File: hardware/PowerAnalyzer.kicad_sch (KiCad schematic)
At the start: 59 parts, among them J1 EXPANSION, J10 TEST_IN, J11 PWR_IN, J12 PWR_OUT, J2 UDPI, J3 I2C, J4 FAN, J5 NTC, J6 UART, J7 USB_C_Receptacle_USB2.0_16P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

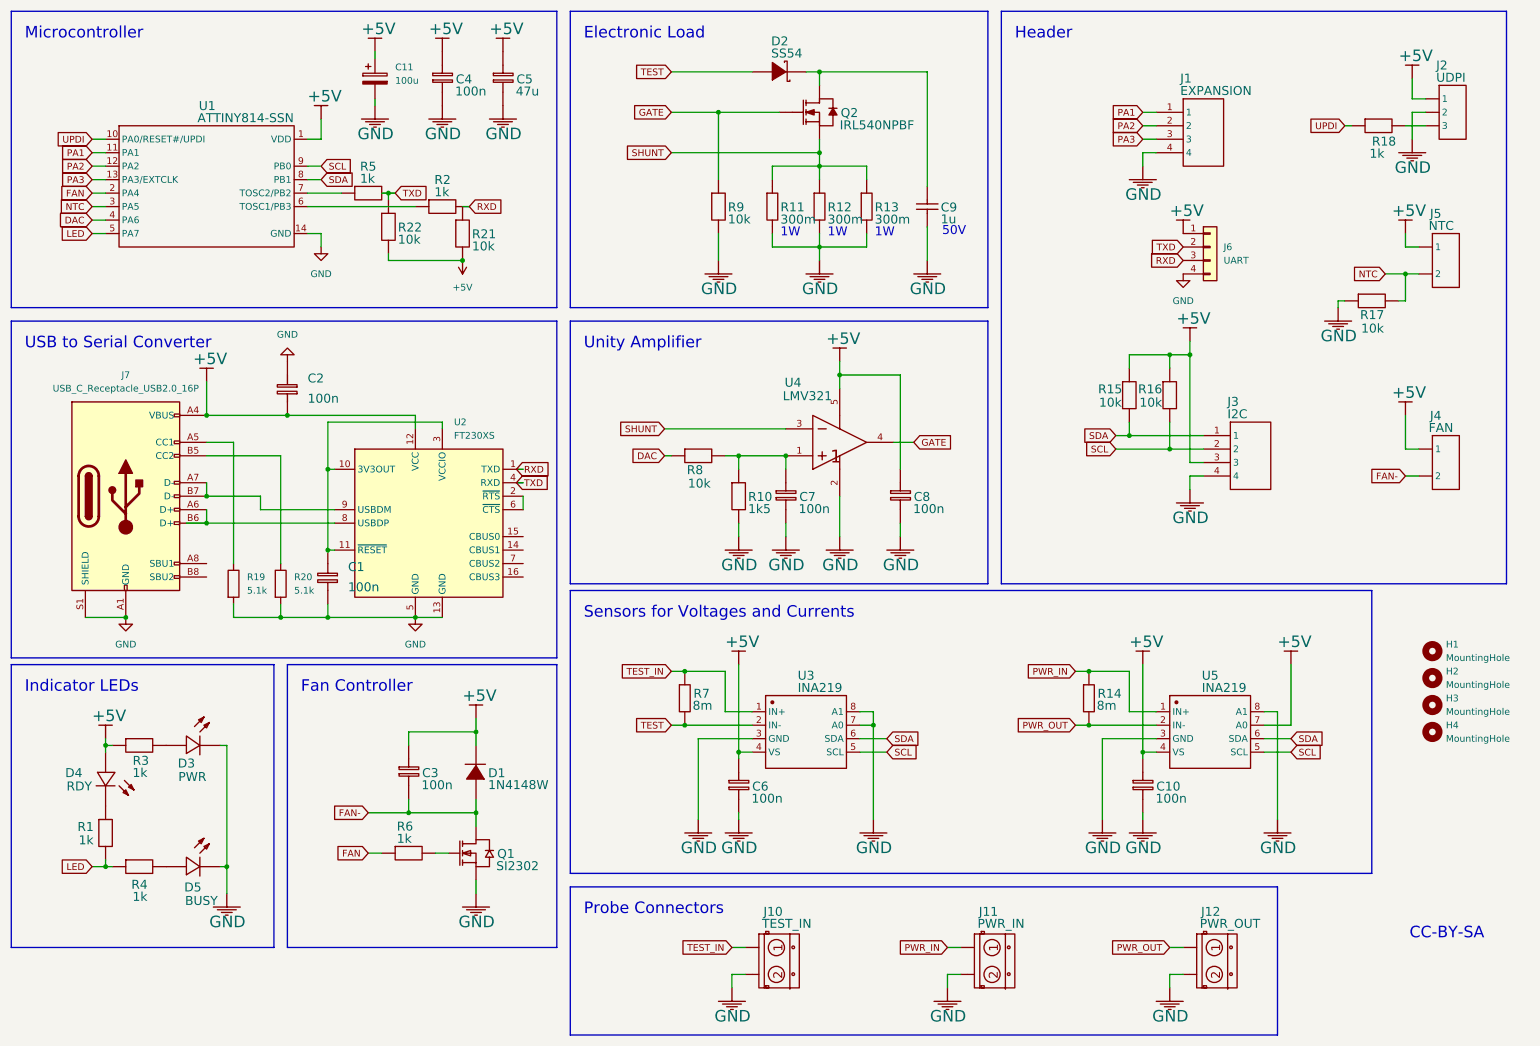
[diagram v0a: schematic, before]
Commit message: Fix diodes
Their pins are numbered differently on easyEDA.
Move some vias which may cause tombstoning.
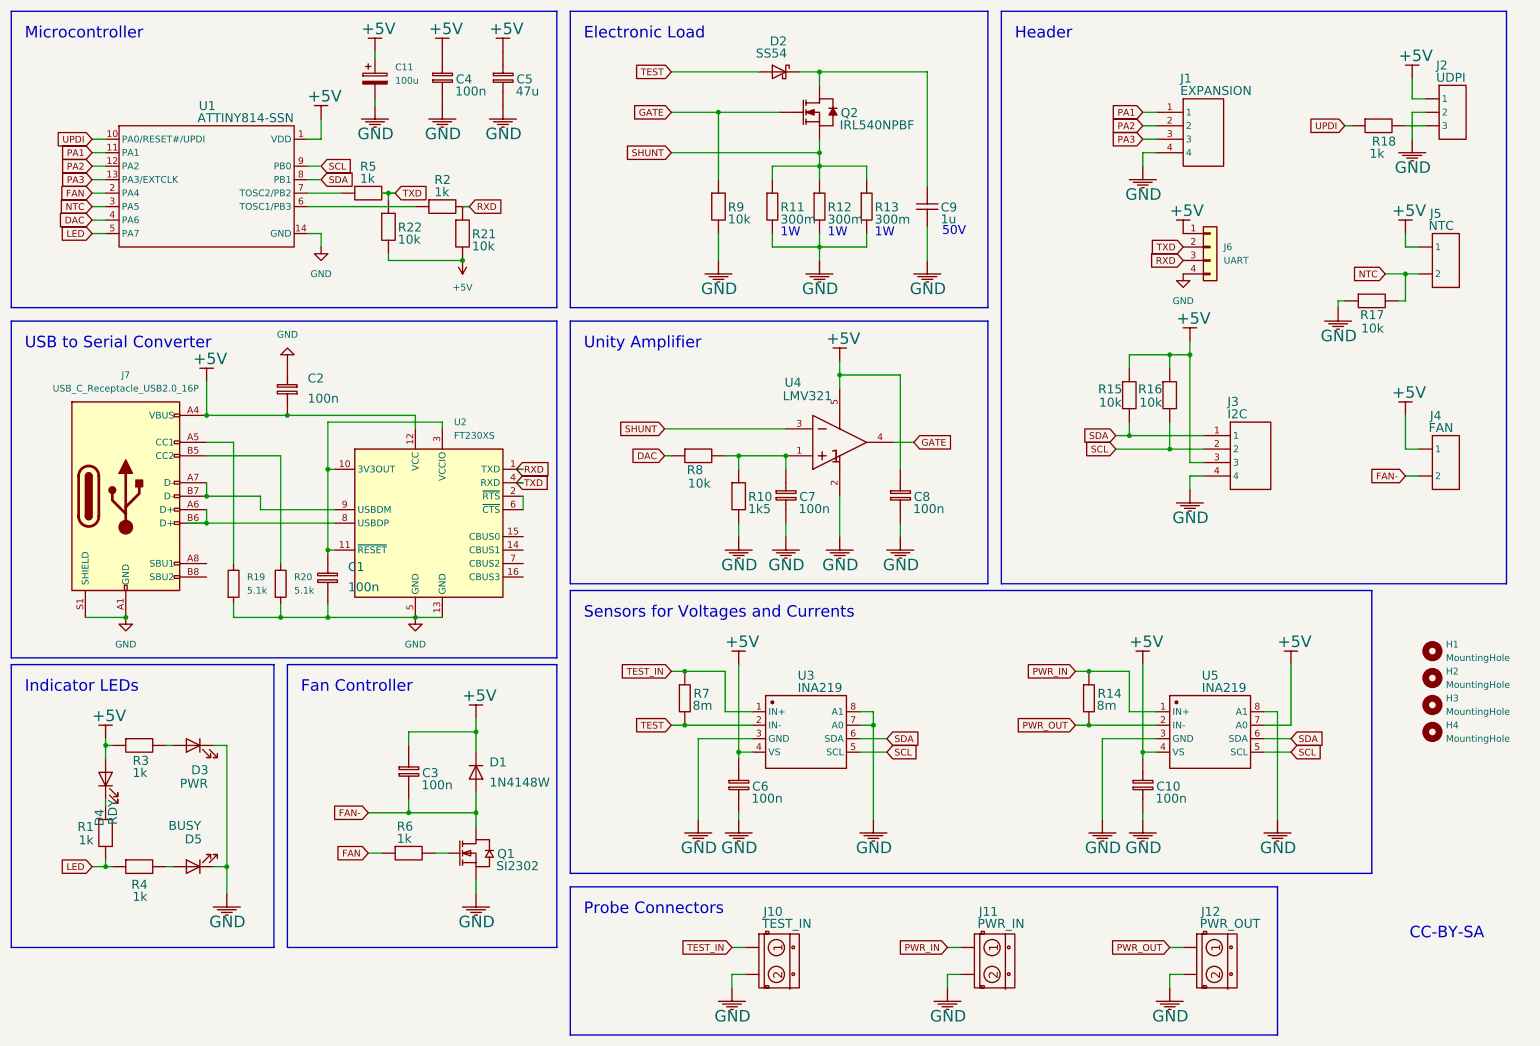
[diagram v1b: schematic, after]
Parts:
- D1: symbol Unknown_365_-270 -> Device:D
- D2: symbol SS54_C123946 -> Device:D_Schottky
- D3: symbol Unknown_155_-295 -> Device:LED
- D4: symbol Unknown_95_-265 -> Device:LED
- D5: symbol Unknown_155_-205 -> Device:LED
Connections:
- net +5V: now also D1.1 (K), D4.2 (A); no longer D1.2 (K), D4.1 (+)
- net FAN-: now also D1.2 (A); no longer D1.1 (A)
- net GND: now also D3.1 (K), D5.1 (K); no longer D3.2 (-), D5.2 (-)
- net TEST: now also D2.2 (A); no longer D2.1 (A)
- net at R3.2: now also D3.2 (A); no longer D3.1 (+)
- net at R1.2: now also D4.1 (K); no longer D4.2 (-)
- net at C9.2, Q2.2 (D): now also D2.1 (K); no longer D2.2 (K)
- net at R4.2: now also D5.2 (A); no longer D5.1 (+)

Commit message: Pocket Power Prowler v2
Migrate from semi-constant current control via shunt and operational
amplifier to direct DAC- and P[ID]-based control algorithm.
Bias the op amp just below the MOSFET threshold voltage to make use of
full DAC range.
Reduce DAC output capacitance from 100 n to 10 p (in order to filter out
high frequencies coming from DAC peripheral clock).

Shield the op amp and the fan controller.

Allow for powering the fan with external power.

Remove the series diode with the load, unsure for the reason of its
existance, but no literature seems to confirm the need for it.

Make the board a tad smaller.
Rebrand!
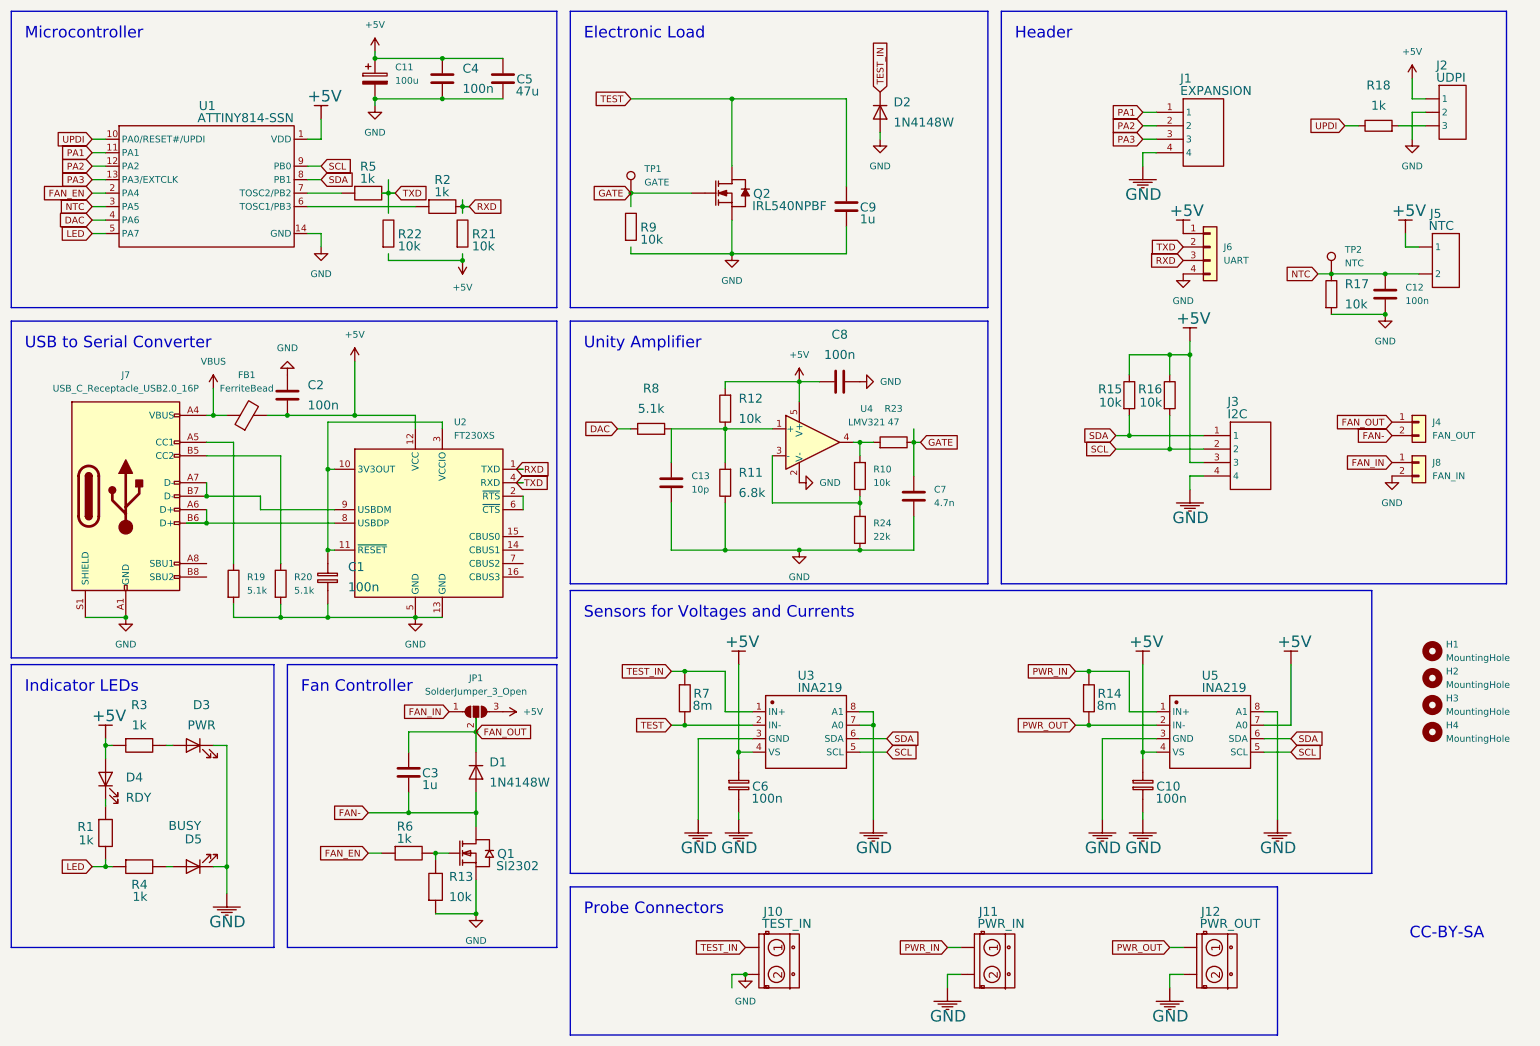
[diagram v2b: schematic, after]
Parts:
- removed C3: 100n, Capacitor_SMD:C_0603_1608Metric, symbol Cap_0603_EU_1
- removed C7: 100n, Capacitor_SMD:C_0603_1608Metric, symbol Cap_0603_EU_4
- removed D2: SS54, Diode_SMD:D_SMA, symbol Device:D_Schottky
- removed J4: FAN, Connector_PinHeader_2.54mm:PinHeader_1x02_P2.54mm_Vertical, symbol Header-Male-2.54_1x2_1
- removed R10: 1k5, Resistor_SMD:R_0603_1608Metric, symbol Res_0603(1/10W)_EU_12
- removed R11: 300m, Resistor_SMD:R_2512_6332Metric, symbol CR2512F0R3E04_2
- removed R12: 300m, Resistor_SMD:R_2512_6332Metric, symbol CR2512F0R3E04_1
- removed R13: 300m, Resistor_SMD:R_2512_6332Metric, symbol CR2512F0R3E04
- removed U4: LMV321, Package_TO_SOT_SMD:SOT-23-5, symbol LMV321B-TR
- added C12: 100n, Capacitor_SMD:C_0603_1608Metric, symbol Device:C
- added C13: 10p, Capacitor_SMD:C_0603_1608Metric, symbol Device:C
- added C3: 1u, Capacitor_SMD:C_0603_1608Metric, symbol Device:C
- added C7: 4.7n, Capacitor_SMD:C_0603_1608Metric, symbol Device:C
- added D2: 1N4148W, Diode_SMD:D_SOD-123, symbol Device:D
- added FB1: FerriteBead, Inductor_SMD:L_0603_1608Metric, symbol Device:FerriteBead
- added J4: FAN_OUT, Connector_PinHeader_2.54mm:PinHeader_1x02_P2.54mm_Vertical, symbol Connector_Generic:Conn_01x02
- added J8: FAN_IN, Connector_PinHeader_2.54mm:PinHeader_1x02_P2.54mm_Vertical, symbol Connector_Generic:Conn_01x02
- added JP1: SolderJumper_3_Open, Jumper:SolderJumper-3_P1.3mm_Open_RoundedPad1.0x1.5mm, symbol Jumper:SolderJumper_3_Open
- added R10, R12: 10k, Resistor_SMD:R_0603_1608Metric, symbol Device:R
- added R11: 6.8k, Resistor_SMD:R_0603_1608Metric, symbol Device:R
- added R13: 10k, Resistor_SMD:R_0603_1608Metric, symbol Res_0603(1/10W)_EU_5
- added R23: 47, Resistor_SMD:R_0603_1608Metric, symbol Device:R
- added R24: 22k, Resistor_SMD:R_0603_1608Metric, symbol Device:R
- added TP1: GATE, TestPoint:TestPoint_Pad_D1.0mm, symbol Connector:TestPoint
- added TP2: NTC, TestPoint:TestPoint_Pad_D1.0mm, symbol Connector:TestPoint
- added U4: LMV321, Package_TO_SOT_SMD:SOT-23-5, symbol Amplifier_Operational:LMV321
- C2: symbol Cap_0603_EU_2 -> Device:C
- C4: symbol Cap_0603_EU -> Device:C
- C5: symbol Cap_1206_EU -> Device:C
- C8: symbol Cap_0603_EU_7 -> Device:C
- C9: symbol UMK107AB7105KA-T -> Device:C; Voltage (none) -> 50V
- R15: symbol Res_0603(1/10W)_EU_6 -> Device:R
- R16: symbol Res_0603(1/10W)_EU_7 -> Device:R
- R17: symbol Res_0603(1/10W)_EU_10 -> Device:R
- R18: symbol Res_0603(1/10W)_EU_2 -> Device:R
- R21, R22, R9: symbol Res_0603(1/10W)_EU_3 -> Device:R
- R8: value 10k -> 5.1k; symbol Res_0603(1/10W)_EU_11 -> Device:R; Manufacturer UniOhm -> (none); Manufacturer Part 0603WAF1002T5E -> (none); Supplier LCSC -> (none); Supplier Part C25804 -> (none)
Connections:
- net SHUNT is gone; now on net GND: Q2.3 (S)
- net +5V: now also R15.1, R16.1, FB1.2, JP1.3 (B), R12.2, U4.5 (V+); no longer D1.1 (K), J7.A4 (VBUS), J7.A9 (VBUS), J7.B4 (VBUS), J7.B9 (VBUS), R15.2, R16.2, R21.1, R22.1
- net DAC: now also R8.1; no longer R8.2
- net FAN-: now also C3.2, J4.2 (Pin_2)
- net GATE: now also C7.1, R23.1, TP1.1; no longer R9.2
- net GND: now also C9.2, C12.1, C13.2, C7.2, D2.2 (A), J8.2 (Pin_2), R11.1, R13.1, R24.1, U4.2 (V-); no longer C9.1, R9.1
- net NTC: now also C12.2, TP2.1
- net RXD: no longer R21.2
- net SCL: now also R16.2; no longer R16.1
- net SDA: now also R15.2; no longer R15.1
- net TEST: now also C9.1, Q2.2 (D)
- net TEST_IN: now also D2.1 (K)
- net TXD: no longer R22.2
- net at Q1.1 (G), R6.2: now also R13.2
- net FAN renamed FAN_EN
- new net: C13.1, R11.2, R12.1, R8.2, U4.1 (+)
- new net: R10.1, R24.2, U4.3 (-)
- new net: R10.2, R23.2, U4.4
- new net FAN_IN: J8.1 (Pin_1), JP1.1 (A)
- new net FAN_OUT: C3.1, D1.1 (K), J4.1 (Pin_1), JP1.2 (C)
- new net VBUS: FB1.1, J7.A4 (VBUS), J7.A9 (VBUS), J7.B4 (VBUS), J7.B9 (VBUS)
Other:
- note removed: "1W"
- note removed: "50V"
- moved on the sheet: Q2

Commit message: Finish (?) KiCadifying
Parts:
- C1: symbol Cap_0603_EU_2 -> Device:C
- C10: symbol Cap_0603_EU_6 -> Device:C
- C6: symbol Cap_0603_EU_5 -> Device:C
- J1: symbol 220S-1*4P H=8.5MM Ytype Gold-plated_1 -> Connector_Generic:Conn_01x04
- J10: symbol Unknown_160_-100 -> Connector:Screw_Terminal_01x02
- J11: symbol Unknown_320_-100 -> Connector:Screw_Terminal_01x02
- J12: symbol Unknown_485_-100 -> Connector:Screw_Terminal_01x02
- J2: symbol Unknown_1085_-710 -> Connector_Generic:Conn_01x03
- J3: symbol 220S-1*4P H=8.5MM Ytype Gold-plated -> Connector_Generic:Conn_01x04
- J5: symbol Header-Male-2.54_1x2 -> Connector_Generic:Conn_01x02
- R1: symbol Res_0603(1/10W)_EU_4 -> Device:R
- R13, R6: symbol Res_0603(1/10W)_EU_5 -> Device:R
- R2: symbol Res_0603(1/10W)_EU_9 -> Device:R
- R3: symbol Res_0603(1/10W)_EU -> Device:R
- R4: symbol Res_0603(1/10W)_EU_1 -> Device:R
- R5: symbol Res_0603(1/10W)_EU_8 -> Device:R
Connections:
- net +5V: no longer C10.1, R3.1
- net GND: no longer C1.1, C10.2
- net LED: no longer R1.1, R4.1
- net at D3.2 (A): no longer R3.2
- net at D4.1 (K): no longer R1.2
- net at U2.10 (3V3OUT), U2.11 (~{RESET}), U2.3 (VCCIO): no longer C1.2
- net at D5.2 (A): no longer R4.2
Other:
- moved on the sheet: R18, R21, R22

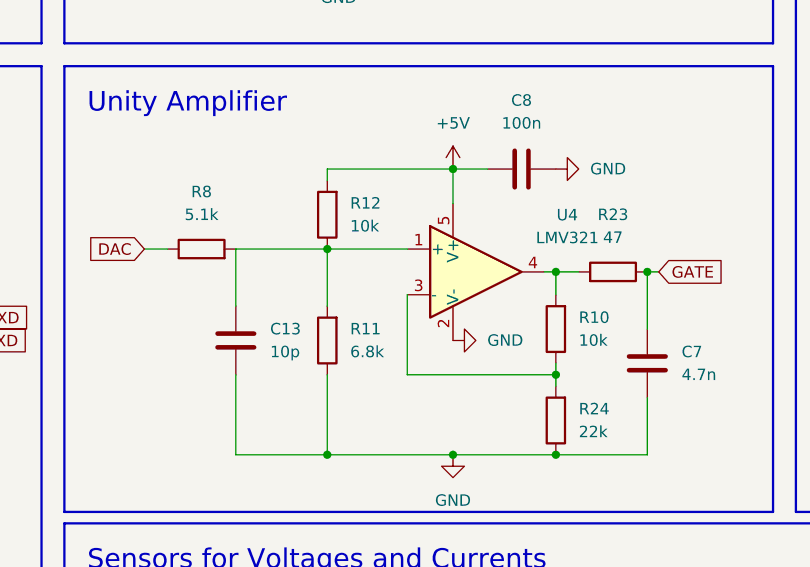
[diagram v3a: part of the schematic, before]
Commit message: Use tried and tested values
Rework on that opamp section sure was fun.
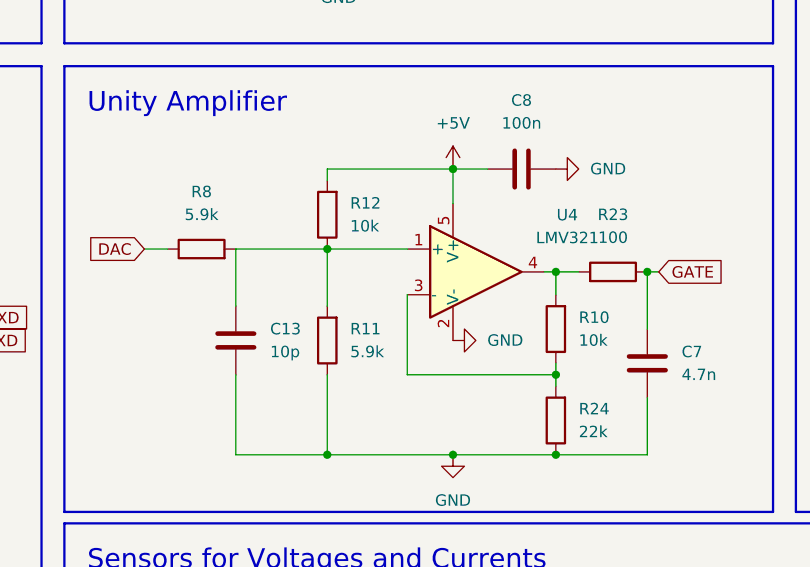
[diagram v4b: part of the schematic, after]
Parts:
- R11: value 6.8k -> 5.9k
- R23: value 47 -> 100
- R8: value 5.1k -> 5.9k
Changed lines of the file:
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@@
 			)
 		)
-		(property "Value" "5.1k"
+		(property "Value" "5.9k"
 			(at 125.73 80.01 90)
 			(effects
@@
 			)
 		)
-		(property "Value" "47"
+		(property "Value" "100"
 			(at 171.45 82.55 90)
 			(effects
@@
 			)
 		)
-		(property "Value" "6.8k"
+		(property "Value" "5.9k"
 			(at 142.24 95.2499 0)
 			(effects
